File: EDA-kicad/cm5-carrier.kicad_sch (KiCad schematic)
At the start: 6 parts

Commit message: delete note
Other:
- note removed: "All resistors/capacitors should be using the package type 0805. This strikes a balance between size and ease of manual repair."

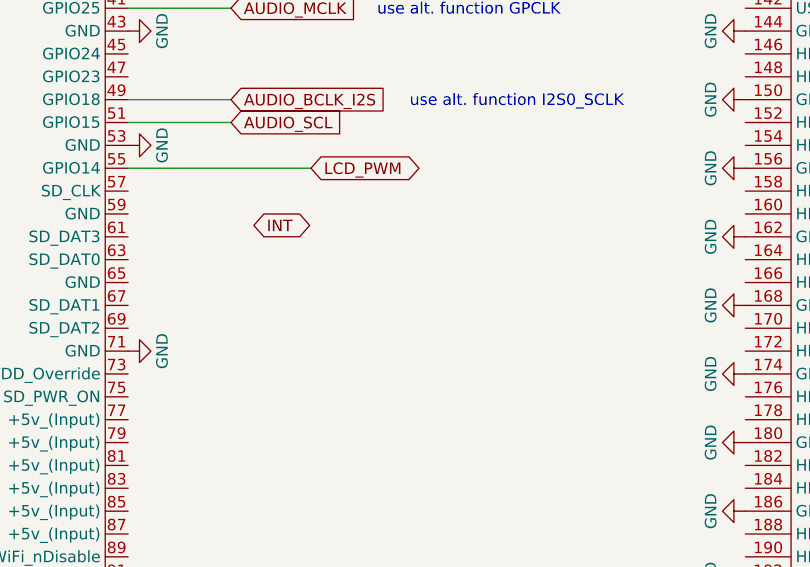
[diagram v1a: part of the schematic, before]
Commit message: organize power related signals
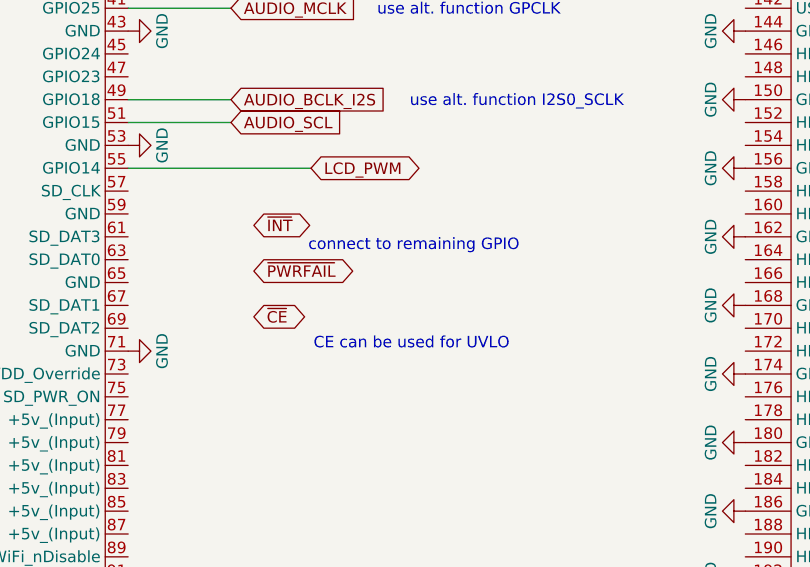
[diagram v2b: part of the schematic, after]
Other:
- note added: "CE can be used for UVLO"
- note added: "connect to remaining GPIO"

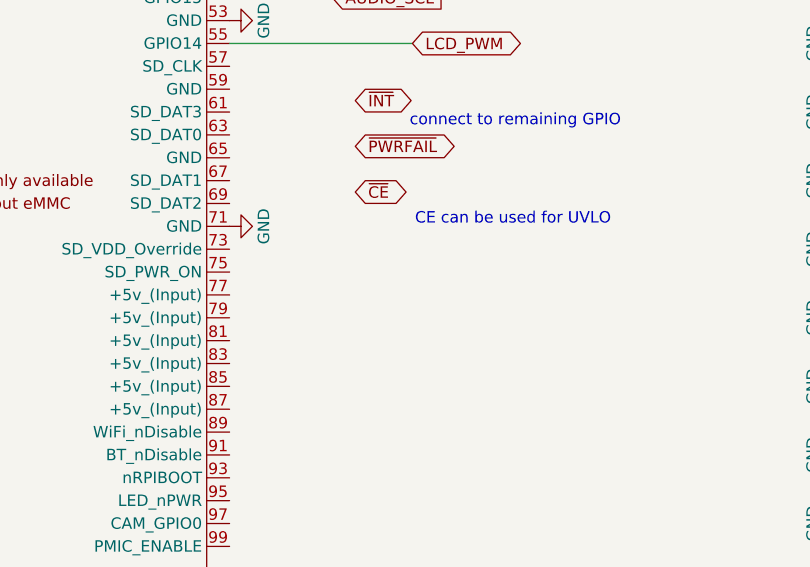
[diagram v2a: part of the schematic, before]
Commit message: separate regulator EN labels for fine grained power saving features etc
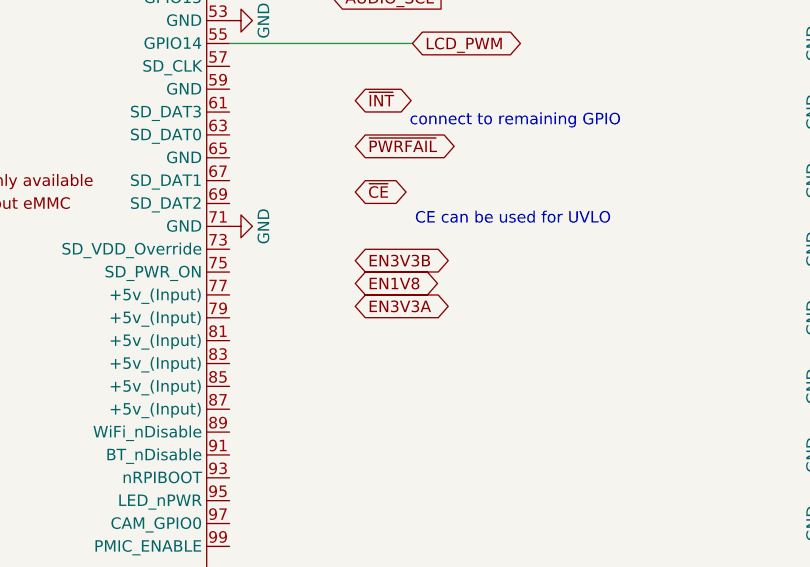
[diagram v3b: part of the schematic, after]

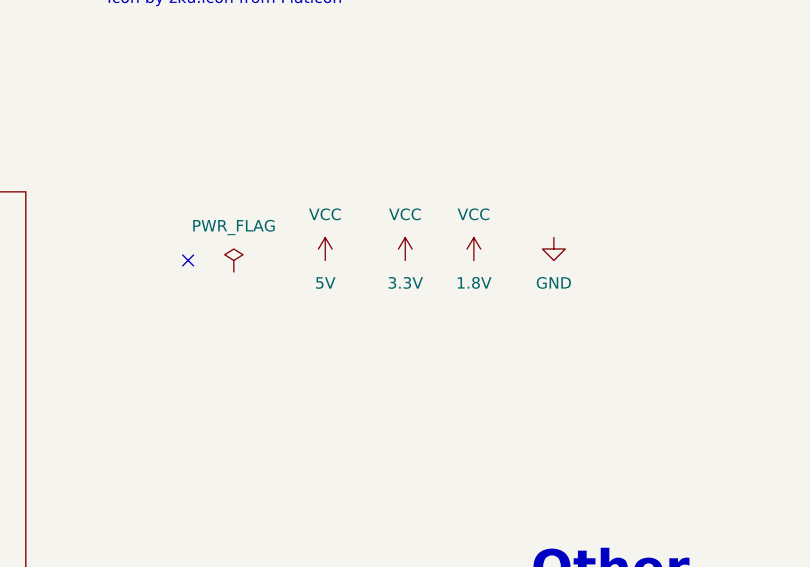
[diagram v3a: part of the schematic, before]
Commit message: reannotate entire schematic
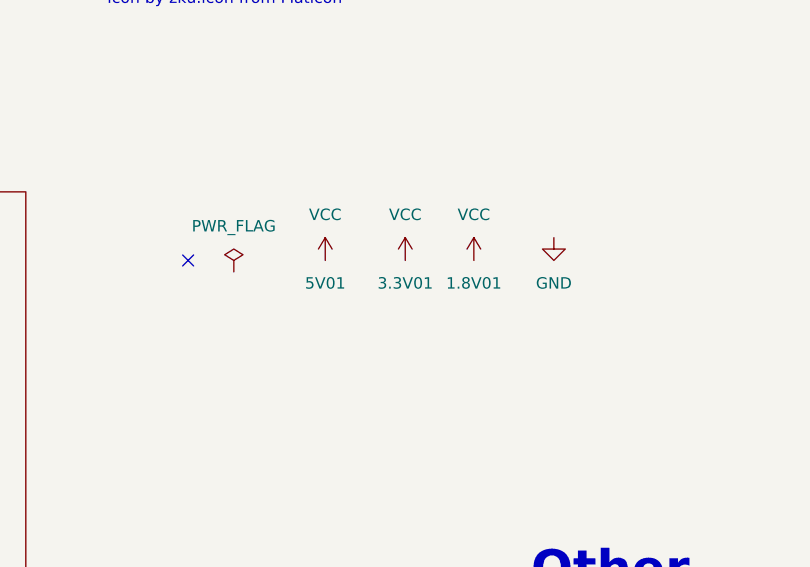
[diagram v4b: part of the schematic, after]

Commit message: add new switches and reannotate
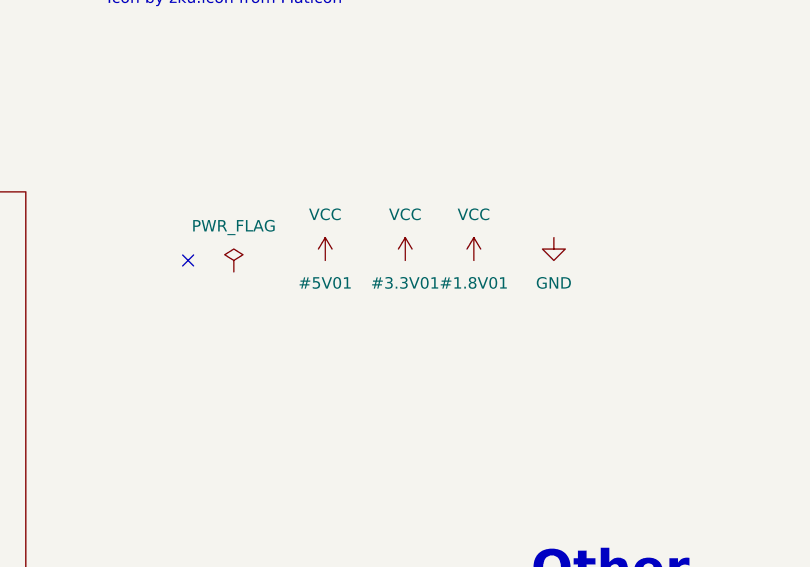
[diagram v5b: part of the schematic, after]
